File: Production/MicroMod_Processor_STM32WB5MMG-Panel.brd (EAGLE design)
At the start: 87.1 x 83.1 mm, 162 parts, among them J1 MICROMOD-2222, J2 MICROMOD-2222, J3 MICROMOD-2222, J4 MICROMOD-2222, J5 MICROMOD-2222, J6 MICROMOD-2222, Q1 20V/4.2A/52mΩ/1.4W, Q2 20V/4.2A/52mΩ/1.4W, Q3 20V/4.2A/52mΩ/1.4W, Q4 20V/4.2A/52mΩ/1.4W, Q5 20V/4.2A/52mΩ/1.4W, Q6 20V/4.2A/52mΩ/1.4W, U1 STM32WB5MMG, U10 W25QXX128MBIT-6X5, U11 STM32WB5MMG, U12 W25QXX128MBIT-6X5, U2 W25QXX128MBIT-6X5, U3 STM32WB5MMG, U4 W25QXX128MBIT-6X5, U5 STM32WB5MMG, U6 W25QXX128MBIT-6X5, U7 STM32WB5MMG, U8 W25QXX128MBIT-6X5, U9 STM32WB5MMG

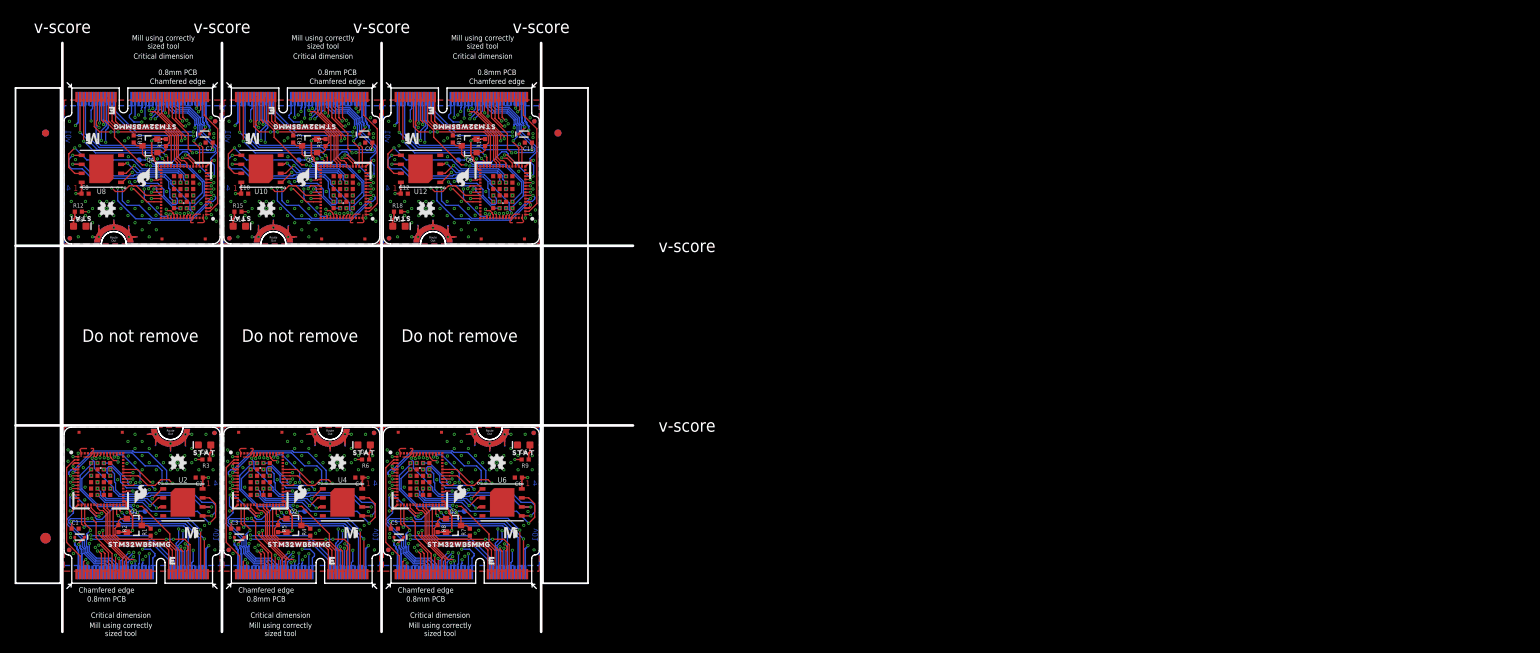
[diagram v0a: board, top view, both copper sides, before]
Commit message: Update for v10
Changelog from v01:
* Connect unused GPIO to ground
** AN4899
** Reduces power consumption and noise
* Add ESD to USB data lines
** This module is sensitive to it
** Moved Flash chip up to make room for ESD diode package
* Set text objects to spin
** When panelizing, the upside down ones didn’t spin on protos so I fixed that
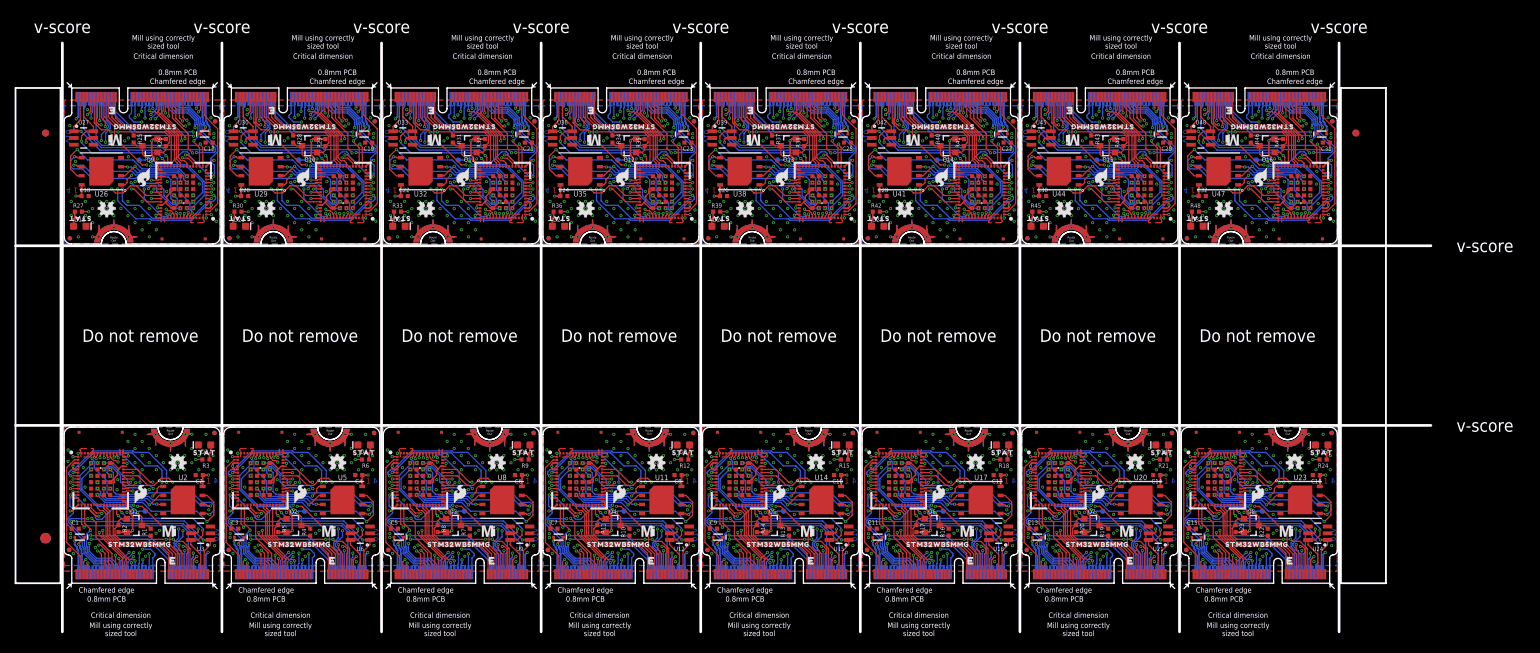
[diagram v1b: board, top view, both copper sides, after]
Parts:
- added C13, C14, C15, C16, C17, C18, C19, C20, C21, C22, C23, C24, C25, C26, C27, C28, C29, C30, C31, C32: 0.1uF, SparkFun-Capacitors:0402-TIGHT
- added D13, D15, D17, D19, D21, D23, D25, D27, D29, D31: 120mA/40V/370mV, SparkFun-DiscreteSemi:SOD-523
- added D14, D16, D18, D20, D22, D24, D26, D28, D30, D32: BLUE, SparkFun-LED:LED-0603
- added FD25, FD26, FD27, FD28, FD29, FD30, FD31, FD32, FD33, FD34, FD35, FD36, FD37, FD38, FD39, FD40, FD41, FD42, FD43, FD44, FD45, FD46, FD47, FD48, FD49, FD50, FD51, FD52, FD53, FD54, FD55, FD56, FD57, FD58, FD59, FD60, FD61, FD62, FD63, FD64: FIDUCIALUFIDUCIAL, SparkFun-Aesthetics:FIDUCIAL-MICRO
- added J10, J11, J12, J13, J14, J15, J16, J7, J8, J9: MICROMOD-2222, SparkFun-MicroMod:M.2-CARD-E-22
- added LOGO19, LOGO22, LOGO25, LOGO28, LOGO31, LOGO34, LOGO37, LOGO40, LOGO43, LOGO46: FOUR_LAYER_WARNING, SparkFun-Aesthetics:FOUR_LAYER_WARNING
- added LOGO20, LOGO23, LOGO26, LOGO29, LOGO32, LOGO35, LOGO38, LOGO41, LOGO44, LOGO47: OSHW-LOGOMINI, SparkFun-Aesthetics:OSHW-LOGO-MINI
- added LOGO21, LOGO24, LOGO27, LOGO30, LOGO33, LOGO36, LOGO39, LOGO42, LOGO45, LOGO48: SFE_LOGO_NAME_FLAME.1_INCH, SparkFun-Aesthetics:SFE_LOGO_NAME_FLAME_.1
- added Q10, Q11, Q12, Q13, Q14, Q15, Q16, Q7, Q8, Q9: 20V/4.2A/52mΩ/1.4W, SparkFun-DiscreteSemi:SOT23-3
- added R19, R20, R22, R23, R25, R26, R28, R29, R31, R32, R34, R35, R37, R38, R40, R41, R43, R44, R46, R47: 100k, SparkFun-Resistors:0402-TIGHT
- added R21, R24, R27, R30, R33, R36, R39, R42, R45, R48: 2.2k, SparkFun-Resistors:0402-TIGHT
- added TP10, TP11, TP12, TP13, TP14, TP15, TP16, TP7, TP8, TP9: TEST-POINT3, SparkFun-Connectors:PAD.03X.03
- added U$100, U$107, U$44, U$51, U$58, U$65, U$72, U$79, U$86, U$93: (no value), SparkFun-MicroMod:MICROMOD_LOGO_.3
- added U$101, U$108, U$45, U$52, U$59, U$66, U$73, U$80, U$87, U$94: (no value), SparkFun-Aesthetics:SFE_LOGO_FLAME_.1
- added U$102, U$103, U$109, U$110, U$46, U$47, U$53, U$54, U$60, U$61, U$67, U$68, U$74, U$75, U$81, U$82, U$88, U$89, U$95, U$96: (no value), output:STM32WB5MMG0
- added U$104, U$111, U$48, U$55, U$62, U$69, U$76, U$83, U$90, U$97: (no value), SparkFun-Aesthetics:SFE_LOGO_FLAME_STOP_.1
- added U$105, U$112, U$49, U$56, U$63, U$70, U$77, U$84, U$91, U$98: (no value), output:STAT0
- added U$106, U$43, U$50, U$57, U$64, U$71, U$78, U$85, U$92, U$99: (no value), SparkFun-MicroMod:MICROMOD_MI_LOGO_.35
- added U13, U16, U19, U22, U25, U28, U31, U34, U37, U40, U43, U46: STM32WB5MMG, stm32wb5mmg:SIP-LGA86
- added U14, U17, U20, U23, U26, U29, U32, U35, U38, U41, U44, U47: W25QXX128MBIT-6X5, SparkFun-IC-Memory:WSON-8-6X5
- added U15, U18, U21, U24, U27, U30, U33, U36, U39, U42, U45, U48: ESD Diode, SparkFun-DiscreteSemi:SOT-23-6
- U10, U4: value W25QXX128MBIT-6X5 -> STM32WB5MMG; device SparkFun-IC-Memory:WSON-8-6X5 -> stm32wb5mmg:SIP-LGA86
- U11, U5: value STM32WB5MMG -> W25QXX128MBIT-6X5; device stm32wb5mmg:SIP-LGA86 -> SparkFun-IC-Memory:WSON-8-6X5
- U12, U6: value W25QXX128MBIT-6X5 -> ESD Diode; device SparkFun-IC-Memory:WSON-8-6X5 -> SparkFun-DiscreteSemi:SOT-23-6
- U3, U9: value STM32WB5MMG -> ESD Diode; device stm32wb5mmg:SIP-LGA86 -> SparkFun-DiscreteSemi:SOT-23-6
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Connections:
- new net !BOOT!10: J11.11, Q11.1, R32.1
- new net !BOOT!11: J12.11, Q12.1, R35.1
- new net !BOOT!12: J13.11, Q13.1, R38.1
- new net !BOOT!13: J14.11, Q14.1, R41.1
- new net !BOOT!14: J15.11, Q15.1, R44.1
- new net !BOOT!15: J16.11, Q16.1, R47.1
- new net !BOOT!6: J7.11, Q7.1, R20.1
- new net !BOOT!7: J8.11, Q8.1, R23.1
- new net !BOOT!8: J9.11, Q9.1, R26.1
- new net !BOOT!9: J10.11, Q10.1, R29.1
- new net !RESET!10: C21.1, J11.6, U31.10
- new net !RESET!11: C23.1, J12.6, U34.10
- new net !RESET!12: C25.1, J13.6, U37.10
- new net !RESET!13: C27.1, J14.6, U40.10
- new net !RESET!14: C29.1, J15.6, U43.10
- new net !RESET!15: C31.1, J16.6, U46.10
- new net !RESET!6: C13.1, J7.6, U19.10
- new net !RESET!7: C15.1, J8.6, U22.10
- new net !RESET!8: C17.1, J9.6, U25.10
- new net !RESET!9: C19.1, J10.6, U28.10
- new net 3.3V10: C22.1, D21.A, J11.2, J11.74, Q11.2, R32.2, U31.17, U31.32, U31.4, U31.6, U32.8
- new net 3.3V11: C24.1, D23.A, J12.2, J12.74, Q12.2, R35.2, U34.17, U34.32, U34.4, U34.6, U35.8
- new net 3.3V12: C26.1, D25.A, J13.2, J13.74, Q13.2, R38.2, U37.17, U37.32, U37.4, U37.6, U38.8
- new net 3.3V13: C28.1, D27.A, J14.2, J14.74, Q14.2, R41.2, U40.17, U40.32, U40.4, U40.6, U41.8
- new net 3.3V14: C30.1, D29.A, J15.2, J15.74, Q15.2, R44.2, U43.17, U43.32, U43.4, U43.6, U44.8
- new net 3.3V15: C32.1, D31.A, J16.2, J16.74, Q16.2, R47.2, U46.17, U46.32, U46.4, U46.6, U47.8
- new net 3.3V6: C14.1, D13.A, J7.2, J7.74, Q7.2, R20.2, U19.17, U19.32, U19.4, U19.6, U20.8
- new net 3.3V7: C16.1, D15.A, J8.2, J8.74, Q8.2, R23.2, U22.17, U22.32, U22.4, U22.6, U23.8
- new net 3.3V8: C18.1, D17.A, J9.2, J9.74, Q9.2, R26.2, U25.17, U25.32, U25.4, U25.6, U26.8
- new net 3.3V9: C20.1, D19.A, J10.2, J10.74, Q10.2, R29.2, U28.17, U28.32, U28.4, U28.6, U29.8
- new net A12: J7.34, U19.8
- new net A13: J7.38, U19.7
- new net A14: J8.34, U22.8
- new net A15: J8.38, U22.7
- new net A16: J9.34, U25.8
- new net A17: J9.38, U25.7
- new net A18: J10.34, U28.8
- new net A19: J10.38, U28.7
- new net A20: J11.34, U31.8
- new net A21: J11.38, U31.7
- new net A22: J12.34, U34.8
- new net A23: J12.38, U34.7
- new net A24: J13.34, U37.8
- new net A25: J13.38, U37.7
- new net A26: J14.34, U40.8
- new net A27: J14.38, U40.7
- new net A28: J15.34, U43.8
- new net A29: J15.38, U43.7
- new net A30: J16.34, U46.8
- new net A31: J16.38, U46.7
- new net AUD_BCLK10: J11.50, U31.50
- new net AUD_BCLK11: J12.50, U34.50
- new net AUD_BCLK12: J13.50, U37.50
- new net AUD_BCLK13: J14.50, U40.50
- new net AUD_BCLK14: J15.50, U43.50
- new net AUD_BCLK15: J16.50, U46.50
- new net AUD_BCLK6: J7.50, U19.50
- new net AUD_BCLK7: J8.50, U22.50
- new net AUD_BCLK8: J9.50, U25.50
- new net AUD_BCLK9: J10.50, U28.50
- new net AUD_FSYNC10: J11.52, U31.11
- new net AUD_FSYNC11: J12.52, U34.11
- new net AUD_FSYNC12: J13.52, U37.11
- new net AUD_FSYNC13: J14.52, U40.11
- new net AUD_FSYNC14: J15.52, U43.11
- new net AUD_FSYNC15: J16.52, U46.11
- new net AUD_FSYNC6: J7.52, U19.11
- new net AUD_FSYNC7: J8.52, U22.11
- new net AUD_FSYNC8: J9.52, U25.11
- new net AUD_FSYNC9: J10.52, U28.11
- new net AUD_I2S_IN10: J11.54, U31.19
- new net AUD_I2S_IN11: J12.54, U34.19
- new net AUD_I2S_IN12: J13.54, U37.19
- new net AUD_I2S_IN13: J14.54, U40.19
- new net AUD_I2S_IN14: J15.54, U43.19
- new net AUD_I2S_IN15: J16.54, U46.19
- new net AUD_I2S_IN6: J7.54, U19.19
- new net AUD_I2S_IN7: J8.54, U22.19
- new net AUD_I2S_IN8: J9.54, U25.19
- new net AUD_I2S_IN9: J10.54, U28.19
- new net AUD_I2S_OUT10: J11.56, U31.38
- new net AUD_I2S_OUT11: J12.56, U34.38
- new net AUD_I2S_OUT12: J13.56, U37.38
- new net AUD_I2S_OUT13: J14.56, U40.38
- new net AUD_I2S_OUT14: J15.56, U43.38
- new net AUD_I2S_OUT15: J16.56, U46.38
- new net AUD_I2S_OUT6: J7.56, U19.38
- new net AUD_I2S_OUT7: J8.56, U22.38
- new net AUD_I2S_OUT8: J9.56, U25.38
- new net AUD_I2S_OUT9: J10.56, U28.38
- new net AUD_MCLK10: J11.58, U31.14
- new net AUD_MCLK11: J12.58, U34.14
- new net AUD_MCLK12: J13.58, U37.14
- new net AUD_MCLK13: J14.58, U40.14
- new net AUD_MCLK14: J15.58, U43.14
- new net AUD_MCLK15: J16.58, U46.14
- new net AUD_MCLK6: J7.58, U19.14
- new net AUD_MCLK7: J8.58, U22.14
- new net AUD_MCLK8: J9.58, U25.14
- new net AUD_MCLK9: J10.58, U28.14
- new net BATT_VIN10: J11.49, U31.49
- new net BATT_VIN11: J12.49, U34.49
- new net BATT_VIN12: J13.49, U37.49
- new net BATT_VIN13: J14.49, U40.49
- new net BATT_VIN14: J15.49, U43.49
- new net BATT_VIN15: J16.49, U46.49
- new net BATT_VIN6: J7.49, U19.49
- new net BATT_VIN7: J8.49, U22.49
- new net BATT_VIN8: J9.49, U25.49
- new net BATT_VIN9: J10.49, U28.49
- new net BOOT10: Q11.3, R31.2, TP11.1, U31.13
- new net BOOT11: Q12.3, R34.2, TP12.1, U34.13
- new net BOOT12: Q13.3, R37.2, TP13.1, U37.13
- new net BOOT13: Q14.3, R40.2, TP14.1, U40.13
- new net BOOT14: Q15.3, R43.2, TP15.1, U43.13
- new net BOOT15: Q16.3, R46.2, TP16.1, U46.13
- new net BOOT6: Q7.3, R19.2, TP7.1, U19.13
- new net BOOT7: Q8.3, R22.2, TP8.1, U22.13
- new net BOOT8: Q9.3, R25.2, TP9.1, U25.13
- new net BOOT9: Q10.3, R28.2, TP10.1, U28.13
- new net GND12: C13.2, C14.2, D14.C, J7.1, J7.33, J7.36, J7.39, J7.45, J7.7, J7.75, J7.GND1, J7.GND2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
- new net GND14: C15.2, C16.2, D16.C, J8.1, J8.33, J8.36, J8.39, J8.45, J8.7, J8.75, J8.GND1, J8.GND2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
- new net GND16: C17.2, C18.2, D18.C, J9.1, J9.33, J9.36, J9.39, J9.45, J9.7, J9.75, J9.GND1, J9.GND2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
- new net GND18: C19.2, C20.2, D20.C, J10.1, J10.33, J10.36, J10.39, J10.45, J10.7, J10.75, J10.GND1, J10.GND2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
- new net GND20: C21.2, C22.2, D22.C, J11.1, J11.33, J11.36, J11.39, J11.45, J11.7, J11.75, J11.GND1, J11.GND2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
- new net GND22: C23.2, C24.2, D24.C, J12.1, J12.33, J12.36, J12.39, J12.45, J12.7, J12.75, J12.GND1, J12.GND2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
- new net GND24: C25.2, C26.2, D26.C, J13.1, J13.33, J13.36, J13.39, J13.45, J13.7, J13.75, J13.GND1, J13.GND2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
- new net GND26: C27.2, C28.2, D28.C, J14.1, J14.33, J14.36, J14.39, J14.45, J14.7, J14.75, J14.GND1, J14.GND2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
- new net GND28: C29.2, C30.2, D30.C, J15.1, J15.33, J15.36, J15.39, J15.45, J15.7, J15.75, J15.GND1, J15.GND2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
- new net GND30: C31.2, C32.2, D32.C, J16.1, J16.33, J16.36, J16.39, J16.45, J16.7, J16.75, J16.GND1, J16.GND2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
- new net I2C1_INT10: J11.16, U31.2
- new net I2C1_INT11: J12.16, U34.2
- new net I2C1_INT12: J13.16, U37.2
- new net I2C1_INT13: J14.16, U40.2
- new net I2C1_INT14: J15.16, U43.2
- new net I2C1_INT15: J16.16, U46.2
- new net I2C1_INT6: J7.16, U19.2
- new net I2C1_INT7: J8.16, U22.2
- new net I2C1_INT8: J9.16, U25.2
- new net I2C1_INT9: J10.16, U28.2
- new net I2C1_SCL10: J11.14, U31.39
- new net I2C1_SCL11: J12.14, U34.39
- new net I2C1_SCL12: J13.14, U37.39
- new net I2C1_SCL13: J14.14, U40.39
- new net I2C1_SCL14: J15.14, U43.39
- new net I2C1_SCL15: J16.14, U46.39
- new net I2C1_SCL6: J7.14, U19.39
- new net I2C1_SCL7: J8.14, U22.39
- new net I2C1_SCL8: J9.14, U25.39
- new net I2C1_SCL9: J10.14, U28.39
- new net I2C1_SDA10: J11.12, U31.18
- new net I2C1_SDA11: J12.12, U34.18
- new net I2C1_SDA12: J13.12, U37.18
- new net I2C1_SDA13: J14.12, U40.18
- new net I2C1_SDA14: J15.12, U43.18
- new net I2C1_SDA15: J16.12, U46.18
- new net I2C1_SDA6: J7.12, U19.18
- new net I2C1_SDA7: J8.12, U22.18
- new net I2C1_SDA8: J9.12, U25.18
- new net I2C1_SDA9: J10.12, U28.18
- new net I2C3_SCL10: J10.53, U28.35
- new net I2C3_SCL11: J11.53, U31.35
- new net I2C3_SCL12: J12.53, U34.35
- new net I2C3_SCL13: J13.53, U37.35
- new net I2C3_SCL14: J14.53, U40.35
- new net I2C3_SCL15: J15.53, U43.35
- new net I2C3_SCL16: J16.53, U46.35
- new net I2C3_SCL7: J7.53, U19.35
- new net I2C3_SCL8: J8.53, U22.35
- new net I2C3_SCL9: J9.53, U25.35
- new net I2C3_SDA10: J10.51, U28.37
- new net I2C3_SDA11: J11.51, U31.37
- new net I2C3_SDA12: J12.51, U34.37
- new net I2C3_SDA13: J13.51, U37.37
- new net I2C3_SDA14: J14.51, U40.37
- new net I2C3_SDA15: J15.51, U43.37
- new net I2C3_SDA16: J16.51, U46.37
- new net I2C3_SDA7: J7.51, U19.37
- new net I2C3_SDA8: J8.51, U22.37
- new net I2C3_SDA9: J9.51, U25.37
- new net LP_RX2/DEV_TX10: J10.20, U28.12
- new net LP_RX2/DEV_TX11: J11.20, U31.12
- new net LP_RX2/DEV_TX12: J12.20, U34.12
- new net LP_RX2/DEV_TX13: J13.20, U37.12
- new net LP_RX2/DEV_TX14: J14.20, U40.12
- new net LP_RX2/DEV_TX15: J15.20, U43.12
- new net LP_RX2/DEV_TX16: J16.20, U46.12
- new net LP_RX2/DEV_TX7: J7.20, U19.12
- new net LP_RX2/DEV_TX8: J8.20, U22.12
- new net LP_RX2/DEV_TX9: J9.20, U25.12
- new net LP_TX2/DEV_RX10: J10.22, U28.9
- new net LP_TX2/DEV_RX11: J11.22, U31.9
- new net LP_TX2/DEV_RX12: J12.22, U34.9
- new net LP_TX2/DEV_RX13: J13.22, U37.9
- new net LP_TX2/DEV_RX14: J14.22, U40.9
- new net LP_TX2/DEV_RX15: J15.22, U43.9
- new net LP_TX2/DEV_RX16: J16.22, U46.9
- new net LP_TX2/DEV_RX7: J7.22, U19.9
- new net LP_TX2/DEV_RX8: J8.22, U22.9
- new net LP_TX2/DEV_RX9: J9.22, U25.9
- new net N$10: J5.9, U15.5
- new net N$12: J6.9, U18.5
- new net N$13: D14.A, R21.1
- new net N$14: J7.9, U21.5
- new net N$15: D16.A, R24.1
- new net N$16: J8.9, U24.5
- new net N$17: D18.A, R27.1
- new net N$18: J9.9, U27.5
- new net N$19: D20.A, R30.1
- new net N$2: J1.9, U3.5
- new net N$20: J10.9, U30.5
- new net N$21: D22.A, R33.1
- new net N$22: J11.9, U33.5
- new net N$23: D24.A, R36.1
- new net N$24: J12.9, U36.5
- new net N$25: D26.A, R39.1
- new net N$26: J13.9, U39.5
- new net N$27: D28.A, R42.1
- new net N$28: J14.9, U42.5
- new net N$29: D30.A, R45.1
- new net N$30: J15.9, U45.5
- new net N$31: D32.A, R48.1
- new net N$32: J16.9, U48.5
- new net N$4: J2.9, U6.5
- new net N$6: J3.9, U9.5
- new net N$8: J4.9, U12.5
- new net PA0/G10: J10.73, U28.3
- new net PA0/G11: J11.73, U31.3
- new net PA0/G12: J12.73, U34.3
- new net PA0/G13: J13.73, U37.3
- new net PA0/G14: J14.73, U40.3
- new net PA0/G15: J15.73, U43.3
- new net PA0/G16: J16.73, U46.3
- new net PA0/G7: J7.73, U19.3
- new net PA0/G8: J8.73, U22.3
- new net PA0/G9: J9.73, U25.3
- new net PC11/G10: J10.42, U28.23
- new net PC11/G11: J11.42, U31.23
- new net PC11/G12: J12.42, U34.23
- new net PC11/G13: J13.42, U37.23
- new net PC11/G14: J14.42, U40.23
- new net PC11/G15: J15.42, U43.23
- new net PC11/G16: J16.42, U46.23
- new net PC11/G7: J7.42, U19.23
- new net PC11/G8: J8.42, U22.23
- new net PC11/G9: J9.42, U25.23
- new net PC13/G10: J10.44, U28.40
- new net PC13/G11: J11.44, U31.40
- new net PC13/G12: J12.44, U34.40
- new net PC13/G13: J13.44, U37.40
- new net PC13/G14: J14.44, U40.40
- new net PC13/G15: J15.44, U43.40
- new net PC13/G16: J16.44, U46.40
- new net PC13/G7: J7.44, U19.40
- new net PC13/G8: J8.44, U22.40
- new net PC13/G9: J9.44, U25.40
- new net PD8/G10: J10.46, U28.75
- new net PD8/G11: J11.46, U31.75
- new net PD8/G12: J12.46, U34.75
- new net PD8/G13: J13.46, U37.75
- new net PD8/G14: J14.46, U40.75
- new net PD8/G15: J15.46, U43.75
- new net PD8/G16: J16.46, U46.75
- new net PD8/G7: J7.46, U19.75
- new net PD8/G8: J8.46, U22.75
- new net PD8/G9: J9.46, U25.75
- new net PE3/G10: J10.48, U28.72
- new net PE3/G11: J11.48, U31.72
- new net PE3/G12: J12.48, U34.72
- new net PE3/G13: J13.48, U37.72
- new net PE3/G14: J14.48, U40.72
- new net PE3/G15: J15.48, U43.72
- new net PE3/G16: J16.48, U46.72
- new net PE3/G7: J7.48, U19.72
- new net PE3/G8: J8.48, U22.72
- new net PE3/G9: J9.48, U25.72
- new net PE4/G10: J11.40, U31.42
- new net PE4/G11: J12.40, U34.42
- new net PE4/G12: J13.40, U37.42
- new net PE4/G13: J14.40, U40.42
- new net PE4/G14: J15.40, U43.42
- new net PE4/G15: J16.40, U46.42
- new net PE4/G6: J7.40, U19.42
- new net PE4/G7: J8.40, U22.42
- new net PE4/G8: J9.40, U25.42
- new net PE4/G9: J10.40, U28.42
- new net PH0/G10: J10.69, U28.61
- new net PH0/G11: J11.69, U31.61
- new net PH0/G12: J12.69, U34.61
- new net PH0/G13: J13.69, U37.61
- new net PH0/G14: J14.69, U40.61
- new net PH0/G15: J15.69, U43.61
- new net PH0/G16: J16.69, U46.61
- new net PH0/G6: J7.69, U19.61
- new net PH0/G8: J8.69, U22.61
- new net PH0/G9: J9.69, U25.61
- new net PH1/G10: J10.71, U28.62
- new net PH1/G11: J11.71, U31.62
- new net PH1/G12: J12.71, U34.62
- new net PH1/G13: J13.71, U37.62
- new net PH1/G14: J14.71, U40.62
- new net PH1/G15: J15.71, U43.62
- new net PH1/G16: J16.71, U46.62
- new net PH1/G7: J7.71, U19.62
- new net PH1/G8: J8.71, U22.62
- new net PH1/G9: J9.71, U25.62
- new net PWM12: J7.32, U19.63
- new net PWM13: J7.47, U19.76
- new net PWM14: J8.32, U22.63
- new net PWM15: J8.47, U22.76
- new net PWM16: J9.32, U25.63
- new net PWM17: J9.47, U25.76
- new net PWM18: J10.32, U28.63
- new net PWM19: J10.47, U28.76
- new net PWM20: J11.32, U31.63
- new net PWM21: J11.47, U31.76
- new net PWM22: J12.32, U34.63
- new net PWM23: J12.47, U34.76
- new net PWM24: J13.32, U37.63
- new net PWM25: J13.47, U37.76
- new net PWM26: J14.32, U40.63
- new net PWM27: J14.47, U40.76
- new net PWM28: J15.32, U43.63
- new net PWM29: J15.47, U43.76
- new net PWM30: J16.32, U46.63
- new net PWM31: J16.47, U46.76
- new net QSPI_!CS!10: U31.70, U32.1
- new net QSPI_!CS!11: U34.70, U35.1
- new net QSPI_!CS!12: U37.70, U38.1
- new net QSPI_!CS!13: U40.70, U41.1
- new net QSPI_!CS!14: U43.70, U44.1
- new net QSPI_!CS!15: U46.70, U47.1
- new net QSPI_!CS!6: U19.70, U20.1
- new net QSPI_!CS!7: U22.70, U23.1
- new net QSPI_!CS!8: U25.70, U26.1
- new net QSPI_!CS!9: U28.70, U29.1
- new net QSPI_CLK10: U31.56, U32.6
- new net QSPI_CLK11: U34.56, U35.6
- new net QSPI_CLK12: U37.56, U38.6
- new net QSPI_CLK13: U40.56, U41.6
- new net QSPI_CLK14: U43.56, U44.6
- new net QSPI_CLK15: U46.56, U47.6
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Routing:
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- added copper zone on layer 15, net 3.3V10
- added copper zone on layer 15, net 3.3V11
- added copper zone on layer 15, net 3.3V12
- added copper zone on layer 15, net 3.3V13
- added copper zone on layer 15, net 3.3V14
- added copper zone on layer 15, net 3.3V15
- added copper zone on layer 15, net 3.3V6
- added copper zone on layer 15, net 3.3V7
- added copper zone on layer 15, net 3.3V8
- added copper zone on layer 15, net 3.3V9
- added copper zone on layer 1, net GND12
- added copper zone on layer 16, net GND12
- added copper zone on layer 2, net GND12
- added copper zone on layer 15, net GND13
- added copper zone on layer 1, net GND14
- added copper zone on layer 16, net GND14
- added copper zone on layer 2, net GND14
- added copper zone on layer 15, net GND15
- added copper zone on layer 1, net GND16
- added copper zone on layer 16, net GND16
- added copper zone on layer 2, net GND16
- added copper zone on layer 15, net GND17
- added copper zone on layer 1, net GND18
- added copper zone on layer 16, net GND18
- added copper zone on layer 2, net GND18
- added copper zone on layer 15, net GND19
- added copper zone on layer 1, net GND20
- added copper zone on layer 16, net GND20
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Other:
- board size 87.1 x 83.1 mm -> 199.6 x 83.1 mm
- board text added: "Material: TG155"
- board text added: "Solder Mask: Red"
- board text added: "Stackup: JLC7628"
- board text added: "Thickness: 0.8mm"
- board text added: "v10"
- board text removed: "Board Thickness is 0.8mm"
- board text removed: "v01"

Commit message: v10 Update
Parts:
- removed U33, U36, U39, U42, U45, U48: ESD Diode, SparkFun-DiscreteSemi:SOT-23-6
- removed U34, U37, U40, U43, U46: STM32WB5MMG, stm32wb5mmg:SIP-LGA86
- removed U35, U38, U41, U44, U47: W25QXX128MBIT-6X5, SparkFun-IC-Memory:WSON-8-6X5
- added D33, D36, D39, D42, D45, D48: PRTR5V0U2F, SparkFun-IC-Power:SOT886
- added D34, D37, D40, D43, D46: 120mA/40V/370mV, SparkFun-DiscreteSemi:SOD-523
- added D35, D38, D41, D44, D47: BLUE, SparkFun-LED:LED-0603
- D10, D16, D22, D28, D4: value BLUE -> 120mA/40V/370mV; device SparkFun-LED:LED-0603 -> SparkFun-DiscreteSemi:SOD-523
- D11, D17, D23, D29, D5: value 120mA/40V/370mV -> BLUE; device SparkFun-DiscreteSemi:SOD-523 -> SparkFun-LED:LED-0603
- D12, D18, D24, D30, D6: value BLUE -> PRTR5V0U2F; device SparkFun-LED:LED-0603 -> SparkFun-IC-Power:SOT886
- D15, D21, D27, D3, D9: value 120mA/40V/370mV -> PRTR5V0U2F; device SparkFun-DiscreteSemi:SOD-523 -> SparkFun-IC-Power:SOT886
- U10, U16, U22, U28, U4: value STM32WB5MMG -> W25QXX128MBIT-6X5; device stm32wb5mmg:SIP-LGA86 -> SparkFun-IC-Memory:WSON-8-6X5
- U11, U17, U23, U29, U5: value W25QXX128MBIT-6X5 -> STM32WB5MMG; device SparkFun-IC-Memory:WSON-8-6X5 -> stm32wb5mmg:SIP-LGA86
- U12, U18, U24, U30, U6: value ESD Diode -> W25QXX128MBIT-6X5; device SparkFun-DiscreteSemi:SOT-23-6 -> SparkFun-IC-Memory:WSON-8-6X5
- U15, U21, U27, U3, U9: value ESD Diode -> STM32WB5MMG; device SparkFun-DiscreteSemi:SOT-23-6 -> stm32wb5mmg:SIP-LGA86
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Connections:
- new net USBIN_N: D3.4, J1.5
- new net USBIN_N1: D6.4, J2.5
- new net USBIN_N10: D33.4, J11.5
- new net USBIN_N11: D36.4, J12.5
- new net USBIN_N12: D39.4, J13.5
- new net USBIN_N13: D42.4, J14.5
- new net USBIN_N14: D45.4, J15.5
- new net USBIN_N15: D48.4, J16.5
- new net USBIN_N2: D9.4, J3.5
- new net USBIN_N3: D12.4, J4.5
- new net USBIN_N4: D15.4, J5.5
- new net USBIN_N5: D18.4, J6.5
- new net USBIN_N6: D21.4, J7.5
- new net USBIN_N7: D24.4, J8.5
- new net USBIN_N8: D27.4, J9.5
- new net USBIN_N9: D30.4, J10.5
- new net USBIN_P: D3.6, J1.3
- new net USBIN_P1: D6.6, J2.3
- new net USBIN_P10: D33.6, J11.3
- new net USBIN_P11: D36.6, J12.3
- new net USBIN_P12: D39.6, J13.3
- new net USBIN_P13: D42.6, J14.3
- new net USBIN_P14: D45.6, J15.3
- new net USBIN_P15: D48.6, J16.3
- new net USBIN_P2: D9.6, J3.3
- new net USBIN_P3: D12.6, J4.3
- new net USBIN_P4: D15.6, J5.3
- new net USBIN_P5: D18.6, J6.3
- new net USBIN_P6: D21.6, J7.3
- new net USBIN_P7: D24.6, J8.3
- new net USBIN_P8: D27.6, J9.3
- new net USBIN_P9: D30.6, J10.3
- net !RESET!1: now also U3.10; no longer U4.10
- net !RESET!10: now also U21.10; no longer U31.10
- net !RESET!11: now also U23.10; no longer U34.10
- net !RESET!12: now also U25.10; no longer U37.10
- net !RESET!13: now also U27.10; no longer U40.10
- net !RESET!14: now also U29.10; no longer U43.10
- net !RESET!15: now also U31.10; no longer U46.10
- net !RESET!2: now also U5.10; no longer U7.10
- net !RESET!3: now also U7.10; no longer U10.10
- net !RESET!4: now also U9.10; no longer U13.10
- net !RESET!5: now also U11.10; no longer U16.10
- net !RESET!6: now also U13.10; no longer U19.10
- net !RESET!7: now also U15.10; no longer U22.10
- net !RESET!8: now also U17.10; no longer U25.10
- net !RESET!9: now also U19.10; no longer U28.10
- net 3.3V1: now also D4.A, U3.17, U3.32, U3.4, U3.6, U4.8; no longer D3.A, U4.17, U4.32, U4.4, U4.6, U5.8
- net 3.3V10: now also D31.A, U21.17, U21.32, U21.4, U21.6, U22.8; no longer D21.A, U31.17, U31.32, U31.4, U31.6, U32.8
- net 3.3V11: now also D34.A, U23.17, U23.32, U23.4, U23.6, U24.8; no longer D23.A, U34.17, U34.32, U34.4, U34.6, U35.8
- net 3.3V12: now also D37.A, U25.17, U25.32, U25.4, U25.6, U26.8; no longer D25.A, U37.17, U37.32, U37.4, U37.6, U38.8
- net 3.3V13: now also D40.A, U27.17, U27.32, U27.4, U27.6, U28.8; no longer D27.A, U40.17, U40.32, U40.4, U40.6, U41.8
- net 3.3V14: now also D43.A, U29.17, U29.32, U29.4, U29.6, U30.8; no longer D29.A, U43.17, U43.32, U43.4, U43.6, U44.8
- net 3.3V15: now also D46.A, U31.17, U31.32, U31.4, U31.6, U32.8; no longer D31.A, U46.17, U46.32, U46.4, U46.6, U47.8
- net 3.3V2: now also D7.A, U5.17, U5.32, U5.4, U5.6, U6.8; no longer D5.A, U7.17, U7.32, U7.4, U7.6, U8.8
- net 3.3V3: now also D10.A, U7.17, U7.32, U7.4, U7.6, U8.8; no longer D7.A, U10.17, U10.32, U10.4, U10.6, U11.8
- net 3.3V4: now also D13.A, U10.8, U9.17, U9.32, U9.4, U9.6; no longer D9.A, U13.17, U13.32, U13.4, U13.6, U14.8
- net 3.3V5: now also D16.A, U11.17, U11.32, U11.4, U11.6, U12.8; no longer D11.A, U16.17, U16.32, U16.4, U16.6, U17.8
- net 3.3V6: now also D19.A, U13.17, U13.32, U13.4, U13.6, U14.8; no longer D13.A, U19.17, U19.32, U19.4, U19.6, U20.8
- net 3.3V7: now also D22.A, U15.17, U15.32, U15.4, U15.6, U16.8; no longer D15.A, U22.17, U22.32, U22.4, U22.6, U23.8
- net 3.3V8: now also D25.A, U17.17, U17.32, U17.4, U17.6, U18.8; no longer D17.A, U25.17, U25.32, U25.4, U25.6, U26.8
- net 3.3V9: now also D28.A, U19.17, U19.32, U19.4, U19.6, U20.8; no longer D19.A, U28.17, U28.32, U28.4, U28.6, U29.8
- net A10: now also U11.8; no longer U16.8
- net A11: now also U11.7; no longer U16.7
- net A12: now also U13.8; no longer U19.8
- net A13: now also U13.7; no longer U19.7
- net A14: now also U15.8; no longer U22.8
- net A15: now also U15.7; no longer U22.7
- net A16: now also U17.8; no longer U25.8
- net A17: now also U17.7; no longer U25.7
- net A18: now also U19.8; no longer U28.8
- net A19: now also U19.7; no longer U28.7
- net A2: now also U3.8; no longer U4.8
- net A20: now also U21.8; no longer U31.8
- net A21: now also U21.7; no longer U31.7
- net A22: now also U23.8; no longer U34.8
- net A23: now also U23.7; no longer U34.7
- net A24: now also U25.8; no longer U37.8
- net A25: now also U25.7; no longer U37.7
- net A26: now also U27.8; no longer U40.8
- net A27: now also U27.7; no longer U40.7
- net A28: now also U29.8; no longer U43.8
- net A29: now also U29.7; no longer U43.7
- net A3: now also U3.7; no longer U4.7
- net A30: now also U31.8; no longer U46.8
- net A31: now also U31.7; no longer U46.7
- net A4: now also U5.8; no longer U7.8
- net A5: now also U5.7; no longer U7.7
- net A6: now also U7.8; no longer U10.8
- net A7: now also U7.7; no longer U10.7
- net A8: now also U9.8; no longer U13.8
- net A9: now also U9.7; no longer U13.7
- net AUD_BCLK1: now also U3.50; no longer U4.50
- net AUD_BCLK10: now also U21.50; no longer U31.50
- net AUD_BCLK11: now also U23.50; no longer U34.50
- net AUD_BCLK12: now also U25.50; no longer U37.50
- net AUD_BCLK13: now also U27.50; no longer U40.50
- net AUD_BCLK14: now also U29.50; no longer U43.50
- net AUD_BCLK15: now also U31.50; no longer U46.50
- net AUD_BCLK2: now also U5.50; no longer U7.50
- net AUD_BCLK3: now also U7.50; no longer U10.50
- net AUD_BCLK4: now also U9.50; no longer U13.50
- net AUD_BCLK5: now also U11.50; no longer U16.50
- net AUD_BCLK6: now also U13.50; no longer U19.50
- net AUD_BCLK7: now also U15.50; no longer U22.50
- net AUD_BCLK8: now also U17.50; no longer U25.50
- net AUD_BCLK9: now also U19.50; no longer U28.50
- net AUD_FSYNC1: now also U3.11; no longer U4.11
- net AUD_FSYNC10: now also U21.11; no longer U31.11
- net AUD_FSYNC11: now also U23.11; no longer U34.11
- net AUD_FSYNC12: now also U25.11; no longer U37.11
- net AUD_FSYNC13: now also U27.11; no longer U40.11
- net AUD_FSYNC14: now also U29.11; no longer U43.11
- net AUD_FSYNC15: now also U31.11; no longer U46.11
- net AUD_FSYNC2: now also U5.11; no longer U7.11
- net AUD_FSYNC3: now also U7.11; no longer U10.11
- net AUD_FSYNC4: now also U9.11; no longer U13.11
- net AUD_FSYNC5: now also U11.11; no longer U16.11
- net AUD_FSYNC6: now also U13.11; no longer U19.11
- net AUD_FSYNC7: now also U15.11; no longer U22.11
- net AUD_FSYNC8: now also U17.11; no longer U25.11
- net AUD_FSYNC9: now also U19.11; no longer U28.11
- net AUD_I2S_IN1: now also U3.19; no longer U4.19
- net AUD_I2S_IN10: now also U21.19; no longer U31.19
- net AUD_I2S_IN11: now also U23.19; no longer U34.19
- net AUD_I2S_IN12: now also U25.19; no longer U37.19
- net AUD_I2S_IN13: now also U27.19; no longer U40.19
- net AUD_I2S_IN14: now also U29.19; no longer U43.19
- net AUD_I2S_IN15: now also U31.19; no longer U46.19
- net AUD_I2S_IN2: now also U5.19; no longer U7.19
- net AUD_I2S_IN3: now also U7.19; no longer U10.19
- net AUD_I2S_IN4: now also U9.19; no longer U13.19
- net AUD_I2S_IN5: now also U11.19; no longer U16.19
- net AUD_I2S_IN6: now also U13.19; no longer U19.19
- net AUD_I2S_IN7: now also U15.19; no longer U22.19
- net AUD_I2S_IN8: now also U17.19; no longer U25.19
- net AUD_I2S_IN9: now also U19.19; no longer U28.19
- net AUD_I2S_OUT1: now also U3.38; no longer U4.38
- net AUD_I2S_OUT10: now also U21.38; no longer U31.38
- net AUD_I2S_OUT11: now also U23.38; no longer U34.38
- net AUD_I2S_OUT12: now also U25.38; no longer U37.38
- net AUD_I2S_OUT13: now also U27.38; no longer U40.38
- net AUD_I2S_OUT14: now also U29.38; no longer U43.38
- net AUD_I2S_OUT15: now also U31.38; no longer U46.38
- net AUD_I2S_OUT2: now also U5.38; no longer U7.38
- net AUD_I2S_OUT3: now also U7.38; no longer U10.38
- net AUD_I2S_OUT4: now also U9.38; no longer U13.38
- net AUD_I2S_OUT5: now also U11.38; no longer U16.38
- net AUD_I2S_OUT6: now also U13.38; no longer U19.38
- net AUD_I2S_OUT7: now also U15.38; no longer U22.38
- net AUD_I2S_OUT8: now also U17.38; no longer U25.38
- net AUD_I2S_OUT9: now also U19.38; no longer U28.38
- net AUD_MCLK1: now also U3.14; no longer U4.14
- net AUD_MCLK10: now also U21.14; no longer U31.14
- net AUD_MCLK11: now also U23.14; no longer U34.14
- net AUD_MCLK12: now also U25.14; no longer U37.14
- net AUD_MCLK13: now also U27.14; no longer U40.14
- net AUD_MCLK14: now also U29.14; no longer U43.14
- net AUD_MCLK15: now also U31.14; no longer U46.14
- net AUD_MCLK2: now also U5.14; no longer U7.14
- net AUD_MCLK3: now also U7.14; no longer U10.14
- net AUD_MCLK4: now also U9.14; no longer U13.14
- net AUD_MCLK5: now also U11.14; no longer U16.14
- net AUD_MCLK6: now also U13.14; no longer U19.14
- net AUD_MCLK7: now also U15.14; no longer U22.14
- net AUD_MCLK8: now also U17.14; no longer U25.14
- net AUD_MCLK9: now also U19.14; no longer U28.14
- net BATT_VIN1: now also U3.49; no longer U4.49
- net BATT_VIN10: now also U21.49; no longer U31.49
- net BATT_VIN11: now also U23.49; no longer U34.49
- net BATT_VIN12: now also U25.49; no longer U37.49
- net BATT_VIN13: now also U27.49; no longer U40.49
- net BATT_VIN14: now also U29.49; no longer U43.49
- net BATT_VIN15: now also U31.49; no longer U46.49
- net BATT_VIN2: now also U5.49; no longer U7.49
- net BATT_VIN3: now also U7.49; no longer U10.49
- net BATT_VIN4: now also U9.49; no longer U13.49
- net BATT_VIN5: now also U11.49; no longer U16.49
- net BATT_VIN6: now also U13.49; no longer U19.49
- net BATT_VIN7: now also U15.49; no longer U22.49
- net BATT_VIN8: now also U17.49; no longer U25.49
- net BATT_VIN9: now also U19.49; no longer U28.49
- net BOOT1: now also U3.13; no longer U4.13
- net BOOT10: now also U21.13; no longer U31.13
- net BOOT11: now also U23.13; no longer U34.13
- net BOOT12: now also U25.13; no longer U37.13
- net BOOT13: now also U27.13; no longer U40.13
- net BOOT14: now also U29.13; no longer U43.13
- net BOOT15: now also U31.13; no longer U46.13
- net BOOT2: now also U5.13; no longer U7.13
- net BOOT3: now also U7.13; no longer U10.13
- net BOOT4: now also U9.13; no longer U13.13
- net BOOT5: now also U11.13; no longer U16.13
- net BOOT6: now also U13.13; no longer U19.13
- net BOOT7: now also U15.13; no longer U22.13
- net BOOT8: now also U17.13; no longer U25.13
- net BOOT9: now also U19.13; no longer U28.13
- net GND: now also D3.2; no longer U3.2
- net GND10: now also D17.C, D18.2, U11.16, U11.22, U11.24, U11.27, U11.31, U11.33, U11.34, U11.36, U11.43, U11.44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; no longer D12.C, U16.16, U16.22, U16.24, U16.27, U16.31, U16.33, U16.34, U16.36, U16.43, U16.44, U16.45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
- net GND12: now also D20.C, D21.2, U13.16, U13.22, U13.24, U13.27, U13.31, U13.33, U13.34, U13.36, U13.43, U13.44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; no longer D14.C, U19.16, U19.22, U19.24, U19.27, U19.31, U19.33, U19.34, U19.36, U19.43, U19.44, U19.45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
- net GND14: now also D23.C, D24.2, U15.16, U15.22, U15.24, U15.27, U15.31, U15.33, U15.34, U15.36, U15.43, U15.44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; no longer D16.C, U22.16, U22.22, U22.24, U22.27, U22.31, U22.33, U22.34, U22.36, U22.43, U22.44, U22.45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
- net GND16: now also D26.C, D27.2, U17.16, U17.22, U17.24, U17.27, U17.31, U17.33, U17.34, U17.36, U17.43, U17.44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; no longer D18.C, U25.16, U25.22, U25.24, U25.27, U25.31, U25.33, U25.34, U25.36, U25.43, U25.44, U25.45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
- net GND18: now also D29.C, D30.2, U19.16, U19.22, U19.24, U19.27, U19.31, U19.33, U19.34, U19.36, U19.43, U19.44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; no longer D20.C, U28.16, U28.22, U28.24, U28.27, U28.31, U28.33, U28.34, U28.36, U28.43, U28.44, U28.45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
- net GND2: now also D5.C, D6.2, U3.16, U3.22, U3.24, U3.27, U3.31, U3.33, U3.34, U3.36, U3.43, U3.44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; no longer D4.C, U4.16, U4.22, U4.24, U4.27, U4.31, U4.33, U4.34, U4.36, U4.43, U4.44, U4.45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
- net GND20: now also D32.C, D33.2, U21.16, U21.22, U21.24, U21.27, U21.31, U21.33, U21.34, U21.36, U21.43, U21.44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; no longer D22.C, U31.16, U31.22, U31.24, U31.27, U31.31, U31.33, U31.34, U31.36, U31.43, U31.44, U31.45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
- net GND22: now also D35.C, D36.2, U23.16, U23.22, U23.24, U23.27, U23.31, U23.33, U23.34, U23.36, U23.43, U23.44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; no longer D24.C, U34.16, U34.22, U34.24, U34.27, U34.31, U34.33, U34.34, U34.36, U34.43, U34.44, U34.45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
- net GND24: now also D38.C, D39.2, U25.16, U25.22, U25.24, U25.27, U25.31, U25.33, U25.34, U25.36, U25.43, U25.44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; no longer D26.C, U37.16, U37.22, U37.24, U37.27, U37.31, U37.33, U37.34, U37.36, U37.43, U37.44, U37.45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
- net GND26: now also D41.C, D42.2, U27.16, U27.22, U27.24, U27.27, U27.31, U27.33, U27.34, U27.36, U27.43, U27.44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; no longer D28.C, U40.16, U40.22, U40.24, U40.27, U40.31, U40.33, U40.34, U40.36, U40.43, U40.44, U40.45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
- net GND28: now also D44.C, D45.2, U29.16, U29.22, U29.24, U29.27, U29.31, U29.33, U29.34, U29.36, U29.43, U29.44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; no longer D30.C, U43.16, U43.22, U43.24, U43.27, U43.31, U43.33, U43.34, U43.36, U43.43, U43.44, U43.45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
- net GND30: now also D47.C, D48.2, U31.16, U31.22, U31.24, U31.27, U31.31, U31.33, U31.34, U31.36, U31.43, U31.44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; no longer D32.C, U46.16, U46.22, U46.24, U46.27, U46.31, U46.33, U46.34, U46.36, U46.43, U46.44, U46.45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
- net GND4: now also D8.C, D9.2, U5.16, U5.22, U5.24, U5.27, U5.31, U5.33, U5.34, U5.36, U5.43, U5.44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; no longer D6.C, U7.16, U7.22, U7.24, U7.27, U7.31, U7.33, U7.34, U7.36, U7.43, U7.44, U7.45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
- net GND6: now also D11.C, D12.2, U7.16, U7.22, U7.24, U7.27, U7.31, U7.33, U7.34, U7.36, U7.43, U7.44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; no longer D8.C, U10.16, U10.22, U10.24, U10.27, U10.31, U10.33, U10.34, U10.36, U10.43, U10.44, U10.45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
- net GND8: now also D14.C, D15.2, U10.4, U9.16, U9.22, U9.24, U9.27, U9.31, U9.33, U9.34, U9.36, U9.43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; no longer D10.C, U13.16, U13.22, U13.24, U13.27, U13.31, U13.33, U13.34, U13.36, U13.43, U13.44, U13.45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
- net I2C1_INT1: now also U3.2; no longer U4.2
- net I2C1_INT10: now also U21.2; no longer U31.2
- net I2C1_INT11: now also U23.2; no longer U34.2
- net I2C1_INT12: now also U25.2; no longer U37.2
- net I2C1_INT13: now also U27.2; no longer U40.2
- net I2C1_INT14: now also U29.2; no longer U43.2
- net I2C1_INT15: now also U31.2; no longer U46.2
- net I2C1_INT2: now also U5.2; no longer U7.2
- net I2C1_INT3: now also U7.2; no longer U10.2
- net I2C1_INT4: now also U9.2; no longer U13.2
- net I2C1_INT5: now also U11.2; no longer U16.2
- net I2C1_INT6: now also U13.2; no longer U19.2
- net I2C1_INT7: now also U15.2; no longer U22.2
- net I2C1_INT8: now also U17.2; no longer U25.2
- net I2C1_INT9: now also U19.2; no longer U28.2
- net I2C1_SCL1: now also U3.39; no longer U4.39
- net I2C1_SCL10: now also U21.39; no longer U31.39
- net I2C1_SCL11: now also U23.39; no longer U34.39
- net I2C1_SCL12: now also U25.39; no longer U37.39
- net I2C1_SCL13: now also U27.39; no longer U40.39
- net I2C1_SCL14: now also U29.39; no longer U43.39
- net I2C1_SCL15: now also U31.39; no longer U46.39
- net I2C1_SCL2: now also U5.39; no longer U7.39
- net I2C1_SCL3: now also U7.39; no longer U10.39
- net I2C1_SCL4: now also U9.39; no longer U13.39
- net I2C1_SCL5: now also U11.39; no longer U16.39
- net I2C1_SCL6: now also U13.39; no longer U19.39
- net I2C1_SCL7: now also U15.39; no longer U22.39
- net I2C1_SCL8: now also U17.39; no longer U25.39
- net I2C1_SCL9: now also U19.39; no longer U28.39
- net I2C1_SDA1: now also U3.18; no longer U4.18
- net I2C1_SDA10: now also U21.18; no longer U31.18
- net I2C1_SDA11: now also U23.18; no longer U34.18
- net I2C1_SDA12: now also U25.18; no longer U37.18
- net I2C1_SDA13: now also U27.18; no longer U40.18
- net I2C1_SDA14: now also U29.18; no longer U43.18
- net I2C1_SDA15: now also U31.18; no longer U46.18
- net I2C1_SDA2: now also U5.18; no longer U7.18
- net I2C1_SDA3: now also U7.18; no longer U10.18
- net I2C1_SDA4: now also U9.18; no longer U13.18
- net I2C1_SDA5: now also U11.18; no longer U16.18
- net I2C1_SDA6: now also U13.18; no longer U19.18
- net I2C1_SDA7: now also U15.18; no longer U22.18
- net I2C1_SDA8: now also U17.18; no longer U25.18
- net I2C1_SDA9: now also U19.18; no longer U28.18
- net I2C3_SCL10: now also U19.35; no longer U28.35
- net I2C3_SCL11: now also U21.35; no longer U31.35
- net I2C3_SCL12: now also U23.35; no longer U34.35
- net I2C3_SCL13: now also U25.35; no longer U37.35
- net I2C3_SCL14: now also U27.35; no longer U40.35
- net I2C3_SCL15: now also U29.35; no longer U43.35
- net I2C3_SCL16: now also U31.35; no longer U46.35
- net I2C3_SCL2: now also U3.35; no longer U4.35
- net I2C3_SCL3: now also U5.35; no longer U7.35
- net I2C3_SCL4: now also U7.35; no longer U10.35
- net I2C3_SCL5: now also U9.35; no longer U13.35
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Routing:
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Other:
- outline, holes or cut-outs redrawn
